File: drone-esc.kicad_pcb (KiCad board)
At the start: 4 copper layers, 34 x 34 mm, 237 parts, among them J1 SM08B-SRSS-TB_LF__SN_, Q1 IRLHS6242, Q10 IRLHS6242, Q11 IRLHS6242, Q12 IRLHS6242, Q13 IRLHS6242, Q14 IRLHS6242, Q15 IRLHS6242, Q16 IRLHS6242, Q17 IRLHS6242, Q18 IRLHS6242, Q19 IRLHS6242, Q2 IRLHS6242, Q20 IRLHS6242, Q21 IRLHS6242, Q22 IRLHS6242, Q23 IRLHS6242, Q24 IRLHS6242, Q3 IRLHS6242, Q4 IRLHS6242, Q5 IRLHS6242, Q6 IRLHS6242, Q7 IRLHS6242, Q8 IRLHS6242, Q9 IRLHS6242, U10 DGD05473FNQ-7, U11 DGD05473FNQ-7, U12 AT32F421G8U7, U13 DGD05473FNQ-7, U14 DGD05473FNQ-7, U15 DGD05473FNQ-7, U16 AT32F421G8U7, U17 DGD05473FNQ-7, U18 DGD05473FNQ-7, U19 DGD05473FNQ-7, U2 INA186A3IDCKR, U20 AT32F421G8U7, U3 TLV76733DRVR, U4 TPS61023DRLR, U5 AT32F421G8U7, U6 DGD05473FNQ-7, U7 DGD05473FNQ-7, U8 DGD05473FNQ-7, U9 DGD05473FNQ-7

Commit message: 4:24pm 4/29
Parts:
- R1: moved to B.Cu
- moved J1 0.22 mm to (145.0, 78.5)

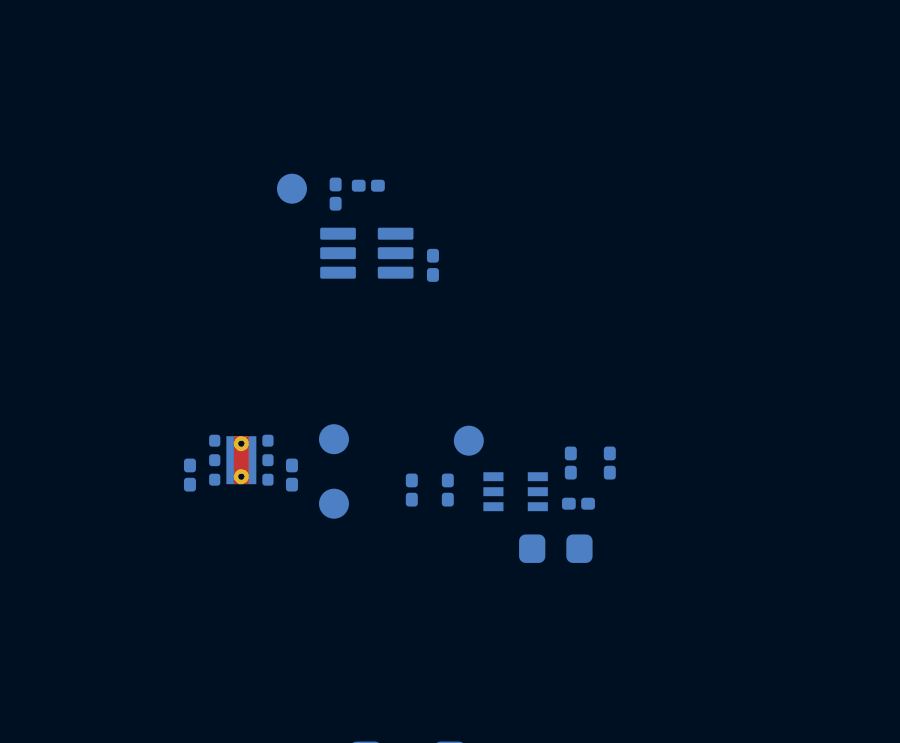
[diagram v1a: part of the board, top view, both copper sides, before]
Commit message: routed power
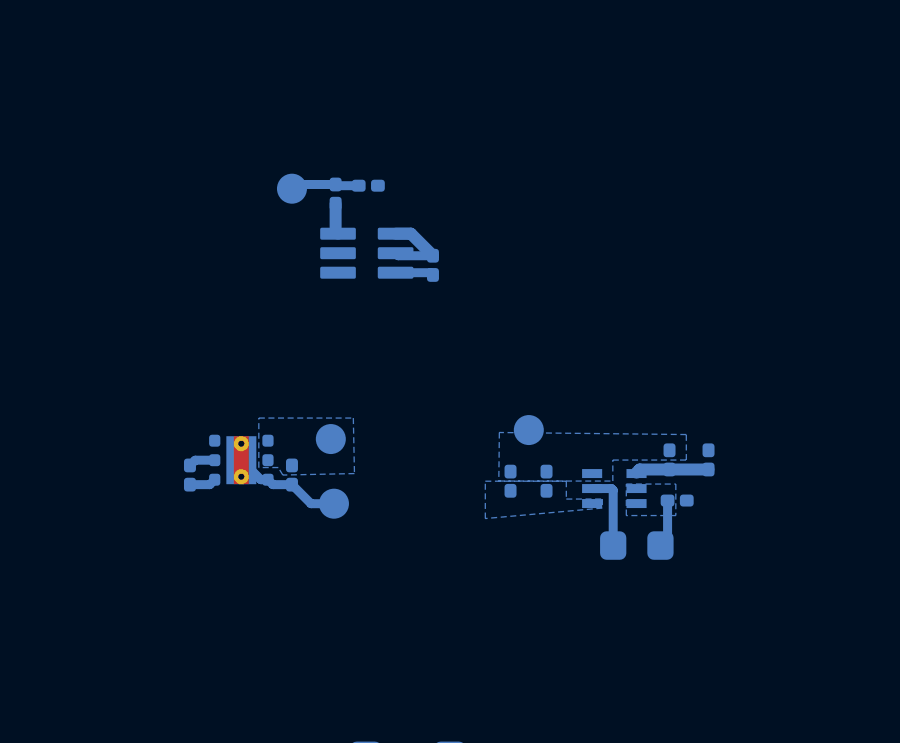
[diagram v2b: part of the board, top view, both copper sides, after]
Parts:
- moved C5 3.30 mm to (149.7, 131.9)
- moved C7 3.30 mm to (148.5, 131.9)
- moved R4 3.29 mm to (155.1, 131.2)
- moved R3 3.29 mm to (153.8, 131.2)
- moved C6 3.29 mm to (154.1, 132.5)
- moved U4 3.29 mm to (152.0, 132.2)
- moved L1 2.70 mm to (152.8, 134.0)
- moved TP17 2.03 mm to (149.2, 130.2)
- moved TP16 0.11 mm to (142.6, 130.5)
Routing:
- net GND: track 0.00 -> 7.42 mm
- net Net-(U4-SW): track 0.00 -> 2.57 mm
- net +BATT: track 0.00 -> 2.49 mm
- net Net-(U4-FB): track 0.00 -> 2.44 mm
- net /CURR: track 0.00 -> 2.30 mm
- net +3.3V: track 0.00 -> 1.28 mm
- net Net-(R2-Pad1): track 0.00 -> 1.03 mm
- added copper zone on B.Cu, net +3.3V
- added copper zone on B.Cu, net +5V
- added copper zone on B.Cu, net +BATT
- added copper zone on B.Cu, net GND
- added copper zone on In1.Cu, net GND

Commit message: half placed
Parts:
- removed TP24, TP25: GAH, TestPoint:TestPoint_Pad_D1.0mm
- removed TP36, TP37: GAL, TestPoint:TestPoint_Pad_D1.0mm
- moved Q10 45.5 mm to (138.1, 99.5)
- moved R36 45.5 mm to (139.3, 96.5)
- moved R37 45.5 mm to (139.9, 100.1)
- moved R40 45.5 mm to (141.1, 100.5)
- moved U10 45.5 mm to (141.4, 97.8)
- moved C34 45.5 mm to (140.9, 97.2)
- moved C38 45.5 mm to (143.5, 96.7)
- moved Q9 45.5 mm to (138.1, 96.8)
- moved R28 45.5 mm to (140.3, 98.8)
- moved R39 45.5 mm to (142.5, 100.5)
- moved R41 45.5 mm to (136.9, 99.5)
- moved Q1 45.4 mm to (135.7, 83.2)
- moved Q2 45.4 mm to (135.7, 85.8)
- moved U6 45.4 mm to (138.9, 84.2)
- moved R53 45.4 mm to (136.9, 82.9)
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
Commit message: main placing
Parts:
- added TP24: GAH, TestPoint:TestPoint_Pad_D1.0mm, F.Cu at (87.3, 62.2)
- added TP25: GAH, TestPoint:TestPoint_Pad_D1.0mm, F.Cu at (92.4, 62.2)
- added TP36: GAL, TestPoint:TestPoint_Pad_D1.0mm, F.Cu at (87.3, 65.2)
- added TP37: GAL, TestPoint:TestPoint_Pad_D1.0mm, F.Cu at (92.4, 65.2)
- R1: moved to F.Cu
- moved TP27 109.6 mm to (86.9, 69.1)
- moved TP39 108.8 mm to (86.9, 72.1)
- moved TP26 93.3 mm to (92.0, 69.1)
- moved TP38 92.5 mm to (92.0, 72.1)
- moved R87 52.6 mm to (154.3, 94.7), turned to 0 degrees
- moved U20 51.9 mm to (149.8, 104.0), turned to 0 degrees
- moved C28 51.5 mm to (145.7, 94.3), turned to 90 degrees
- moved R88 51.0 mm to (155.7, 94.7), turned to 0 degrees
- moved U16 49.7 mm to (148.9, 87.6), turned to 0 degrees
- moved R86 49.1 mm to (156.7, 95.2), turned to 0 degrees
- moved R82 49.0 mm to (146.7, 96.1), turned to 0 degrees
- moved C58 48.7 mm to (153.1, 98.2), turned to 90 degrees
- moved R72 47.8 mm to (156.2, 96.2), turned to -90 degrees
- moved U19 47.5 mm to (155.2, 97.2), turned to 90 degrees
- moved C43 47.4 mm to (148.3, 93.9), turned to 0 degrees
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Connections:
- U1 pad 17: /ESC3/MotorA -> /ESC3/MotorC
- U1 pad 19: /ESC3/MotorC -> /ESC3/MotorA
- U1 pad 20: /ESC4/MotorA -> /ESC4/MotorC
- U1 pad 22: /ESC4/MotorC -> /ESC4/MotorA

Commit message: something
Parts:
- FB1, R6, R7: moved to F.Cu
- moved R4 41.2 mm to (143.9, 91.6), turned to 180 degrees
- moved C6 40.9 mm to (145.3, 92.6), turned to 90 degrees
- moved L1 40.5 mm to (146.8, 94.0), turned to -90 degrees
- moved R3 39.6 mm to (143.9, 92.9), turned to 0 degrees
- moved U4 38.1 mm to (144.9, 94.7), turned to -90 degrees
- moved C5 35.3 mm to (144.6, 97.0), turned to 0 degrees
- moved R47 34.7 mm to (145.8, 88.1), turned to 90 degrees
- moved FB1 34.1 mm to (145.8, 88.8), turned to -90 degrees
- moved C7 34.0 mm to (144.6, 98.2), turned to 0 degrees
- moved R6 33.3 mm to (144.9, 86.3)
- moved TP17 33.2 mm to (142.9, 97.6), turned to -90 degrees
- moved C45 33.1 mm to (145.8, 86.7), turned to 90 degrees
- moved TP15 31.3 mm to (146.2, 101.5), turned to -90 degrees
- moved R7 31.2 mm to (142.8, 84.7)
- moved C25 30.1 mm to (138.8, 88.5)
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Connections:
- U12 pad 10: /ESC2/FBC -> unconnected-(U12-PA4-Pad10)
- U12 pad 9: unconnected-(U12-PA3-Pad9) -> /ESC2/FBC
- U16 pad 10: /ESC3/FBC -> unconnected-(U16-PA4-Pad10)
- U16 pad 9: unconnected-(U16-PA3-Pad9) -> /ESC3/FBC
- U20 pad 10: /ESC4/FBC -> unconnected-(U20-PA4-Pad10)
- U20 pad 9: unconnected-(U20-PA3-Pad9) -> /ESC4/FBC
- U5 pad 10: /ESC1/FBC -> unconnected-(U5-PA4-Pad10)
- U5 pad 9: unconnected-(U5-PA3-Pad9) -> /ESC1/FBC
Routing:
- net /ESC1/ESC_EN: track 0.47 -> 20.4 mm, vias 3 -> 4
- net /ESC1/B_HIGH: track 0.00 -> 7.38 mm, vias 0 -> 2
- net /ESC1/FBC: track 6.59 -> 13.5 mm, vias 1 -> 2
- net /ESC1/B_LOW: track 0.00 -> 6.43 mm, vias 0 -> 2
- net /ESC1/C_LOW: track 0.00 -> 4.90 mm, vias 0 -> 2
- net /ESC1/C_HIGH: track 0.00 -> 4.88 mm, vias 0 -> 2
- net GND: track 7.42 -> 11.5 mm, vias 0 -> 3
- net /M1: track 0.00 -> 3.02 mm, vias 0 -> 1
- net /ESC1/FBA: track 6.85 -> 9.57 mm, vias 1 -> 2
- net /ESC1/A_LOW: track 0.00 -> 2.41 mm, vias 0 -> 2
- net Net-(U5-NRST): track 0.00 -> 2.26 mm
- net Net-(U5-VDDA): track 0.00 -> 1.87 mm, vias 0 -> 1
- net +3.3V: track 1.28 -> 3.01 mm, vias 0 -> 1
- net Net-(U5-PB4): track 0.00 -> 1.06 mm, vias 0 -> 1
- net Net-(U5-BOOT0): track 0.00 -> 0.26 mm, vias 0 -> 1
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- added copper zone on In4.Cu, net GND
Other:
- copper layers 4 -> 6

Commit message: routed motor 1
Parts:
- C36, R30, R31: moved to F.Cu
- moved C16 31.0 mm to (117.2, 112.4)
- moved C17 31.0 mm to (115.2, 112.4)
- moved C18 31.0 mm to (113.2, 112.4)
- moved R31 28.7 mm to (142.8, 101.2)
- moved R26 28.6 mm to (142.8, 102.7), turned to -90 degrees
- moved FB2 28.6 mm to (142.8, 104.2), turned to 90 degrees
- moved C36 26.6 mm to (140.3, 103.5), turned to 180 degrees
- moved R30 26.2 mm to (140.3, 102.8), turned to 0 degrees
- moved C40 23.7 mm to (136.8, 102.5), turned to 90 degrees
- moved C41 22.2 mm to (136.8, 104.0)
- moved U12 0.85 mm to (139.8, 103.3)
- moved U20 0.78 mm to (150.1, 103.2)
- moved R1 0.10 mm to (145.1, 107.0)
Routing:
- net /ESC1/FBCOMMON: track 0.00 -> 22.4 mm, vias 1 -> 3
- net /ESC1/FBB: track 6.91 -> 14.9 mm
- net GND: track 11.5 -> 17.0 mm, vias 3 -> 15
- net /ESC1/A_HIGH: track 0.00 -> 2.42 mm, vias 1 -> 2
- net Net-(U12-NRST): track 0.00 -> 2.33 mm, vias 0 -> 1
- net Net-(U12-BOOT0): track 0.00 -> 1.47 mm, vias 0 -> 1
- net +5V: track 10.7 -> 11.9 mm
- net Net-(U12-VDDA): track 0.00 -> 1.03 mm
- net /ESC1/A_LOW: track 2.41 -> 3.41 mm
- net +3.3V: track 3.01 -> 3.79 mm

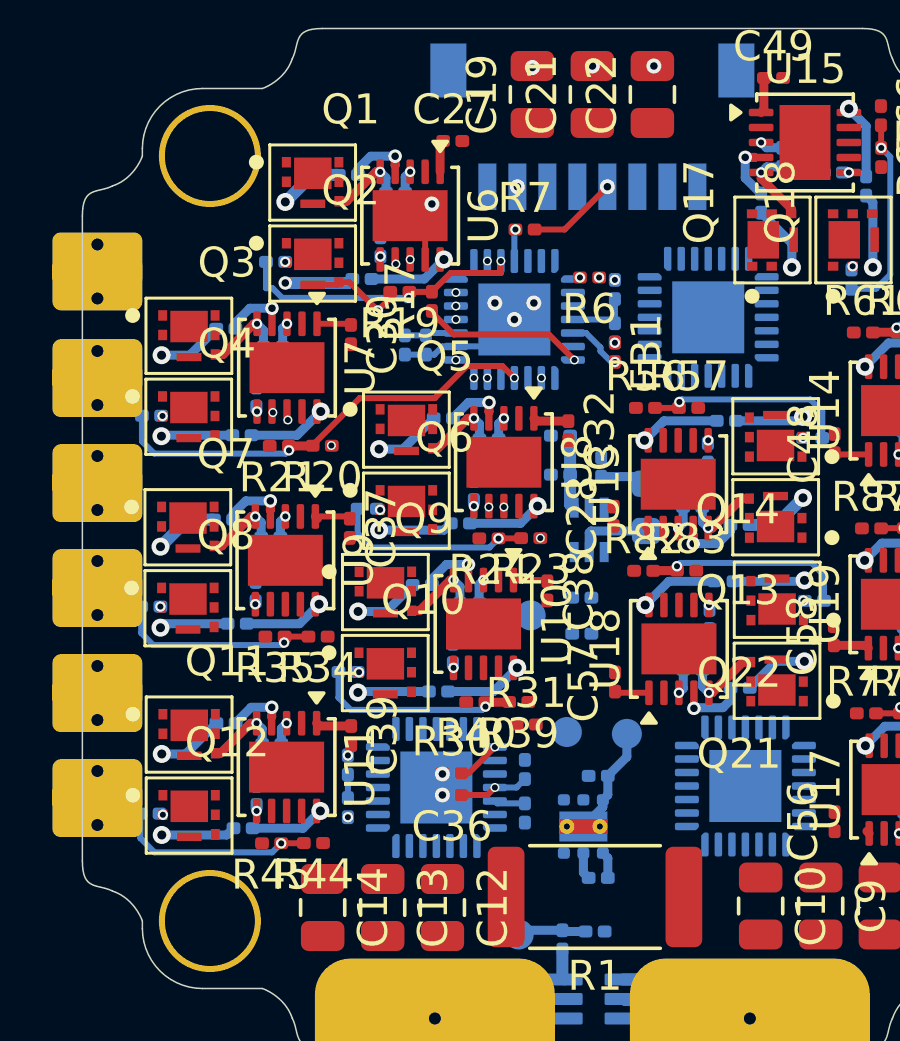
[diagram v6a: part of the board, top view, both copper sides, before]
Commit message: routed motor 2
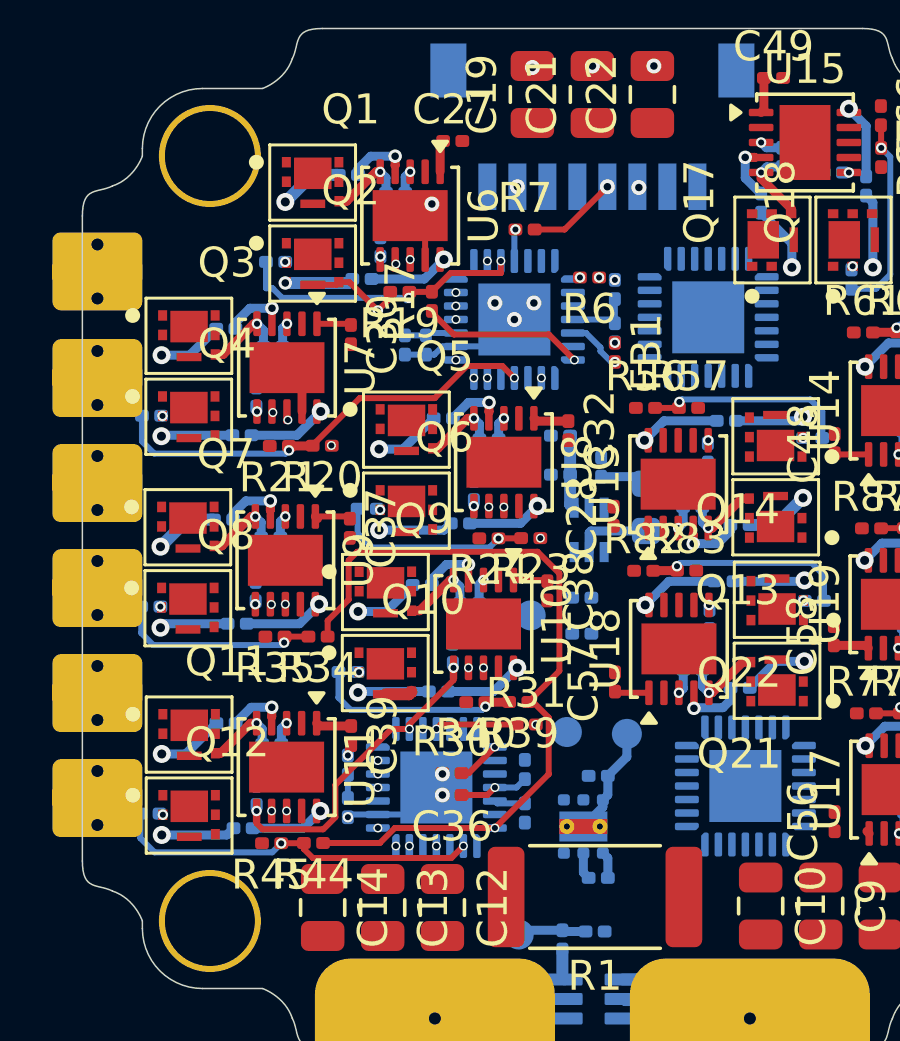
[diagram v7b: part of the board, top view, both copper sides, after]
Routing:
- net /ESC2/FBCOMMON: track 0.00 -> 26.2 mm, vias 0 -> 1
- net /M2: track 0.00 -> 19.3 mm, vias 0 -> 2
- net /ESC2/ESC_EN: track 0.47 -> 18.1 mm, vias 3 -> 4
- net /ESC2/A_LOW: track 0.00 -> 10.7 mm, vias 0 -> 2
- net /ESC2/A_HIGH: track 0.00 -> 8.57 mm, vias 0 -> 2
- net /ESC2/B_LOW: track 0.00 -> 6.90 mm, vias 0 -> 2
- net /ESC2/FBA: track 6.85 -> 12.9 mm, vias 1 -> 2
- net GND: track 17.0 -> 22.9 mm
- net /ESC2/FBC: track 6.59 -> 12.4 mm, vias 1 -> 2
- net /ESC2/B_HIGH: track 0.00 -> 5.59 mm, vias 0 -> 2
- net /ESC2/FBB: track 6.91 -> 12.2 mm, vias 1 -> 2
- net /ESC2/C_LOW: track 0.00 -> 4.81 mm, vias 0 -> 2
- net /ESC2/C_HIGH: track 0.00 -> 4.79 mm, vias 0 -> 2
- net Net-(U12-PB4): track 0.00 -> 2.74 mm, vias 0 -> 1

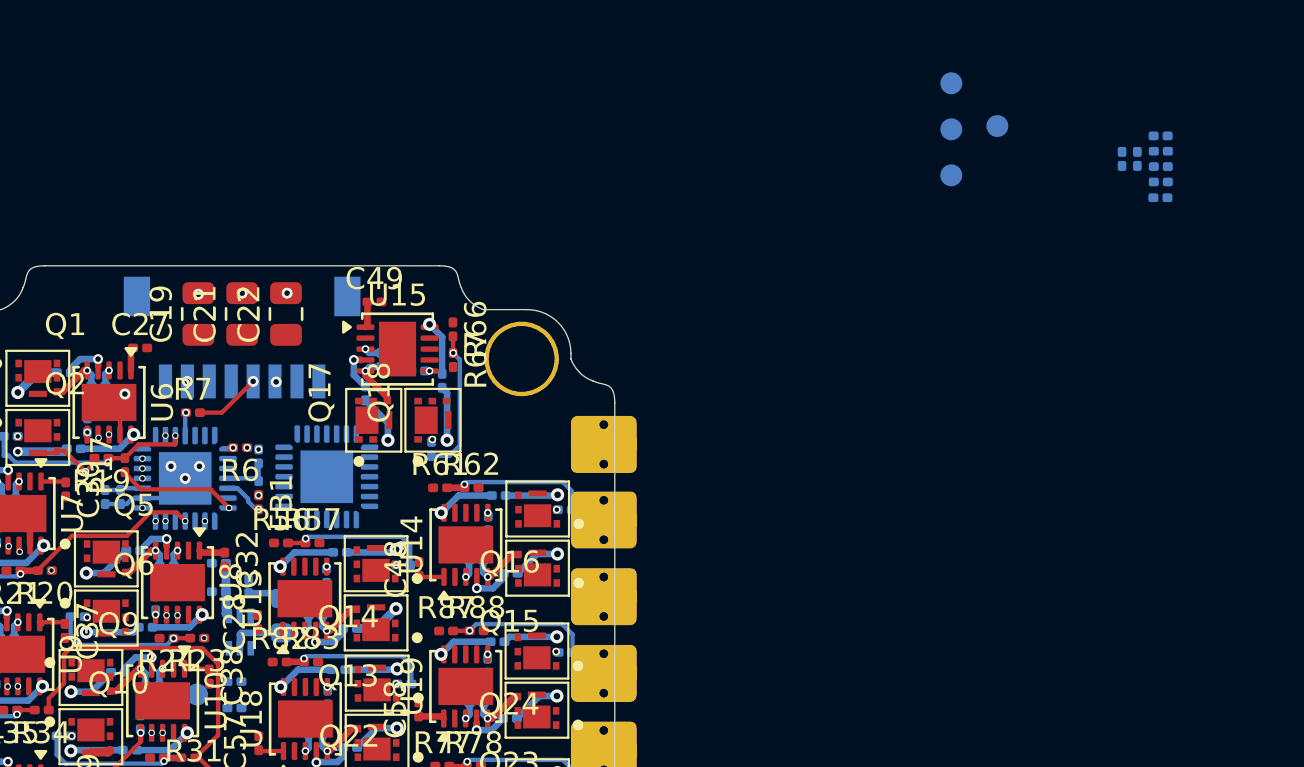
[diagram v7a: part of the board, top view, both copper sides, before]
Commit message: routed motor 3
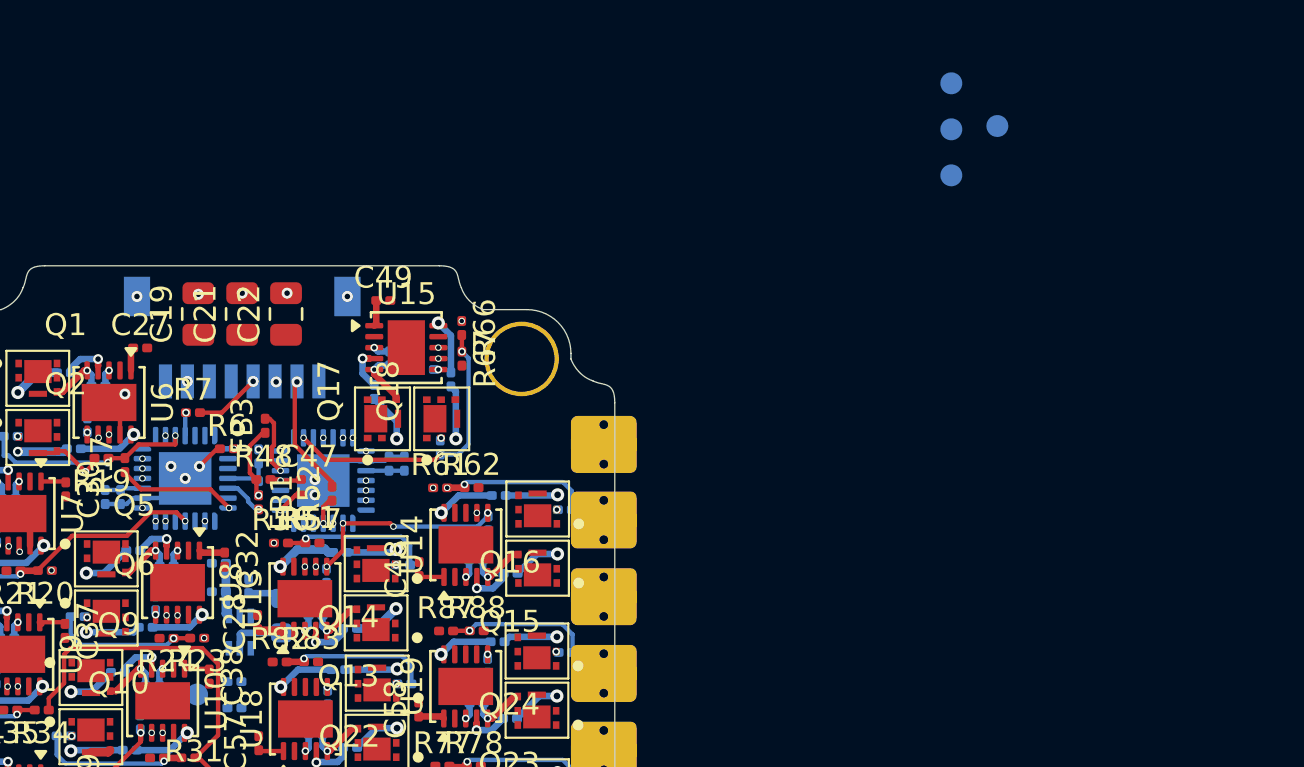
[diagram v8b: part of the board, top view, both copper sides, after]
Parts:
- C47, FB3, R48, R51, R52: moved to F.Cu
- moved R48 43.4 mm to (146.0, 87.8)
- moved FB3 42.9 mm to (146.1, 85.3), turned to 90 degrees
- moved C47 41.7 mm to (148.0, 87.8), turned to 0 degrees
- moved R51 41.5 mm to (148.0, 88.5), turned to 180 degrees
- moved R52 40.1 mm to (149.1, 88.4), turned to 90 degrees
- moved C50 36.2 mm to (152.4, 87.0)
- moved C51 36.2 mm to (151.7, 87.0)
- moved R6 0.60 mm to (144.3, 86.3), turned to 0 degrees
- moved C46 0.41 mm to (151.7, 82.2)
- moved C49 0.41 mm to (151.4, 79.6)
- moved R65 0.41 mm to (154.5, 83.2)
- moved R68 0.41 mm to (154.0, 86.3)
- moved Q18 0.41 mm to (154.1, 85.0)
- moved R50 0.41 mm to (153.4, 82.7)
- moved R64 0.41 mm to (151.0, 83.8)
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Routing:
- net /ESC3/FBCOMMON: track 0.00 -> 22.5 mm, vias 0 -> 4
- net /ESC3/ESC_EN: track 0.47 -> 17.1 mm, vias 3 -> 5
- net /ESC3/FBB: track 6.91 -> 14.7 mm, vias 1 -> 3
- net /ESC3/FBC: track 6.59 -> 13.3 mm, vias 1 -> 3
- net /ESC3/C_LOW: track 0.00 -> 6.14 mm, vias 0 -> 2
- net /ESC3/B_HIGH: track 0.00 -> 6.08 mm, vias 0 -> 2
- net /ESC3/A_LOW: track 0.00 -> 5.59 mm, vias 0 -> 2
- net /M3: track 0.00 -> 5.52 mm, vias 0 -> 1
- net GND: track 22.9 -> 28.3 mm, vias 15 -> 18
- net /ESC3/C_HIGH: track 0.00 -> 5.40 mm, vias 0 -> 2
- net +3.3V: track 3.79 -> 8.91 mm
- net /ESC3/A_HIGH: track 0.00 -> 3.98 mm, vias 0 -> 2
- net Net-(U16-VDDA): track 0.00 -> 2.86 mm, vias 0 -> 1
- net /ESC3/FBA: track 6.85 -> 8.45 mm, vias 1 -> 2
- net Net-(U16-NRST): track 0.00 -> 1.43 mm, vias 0 -> 1
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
